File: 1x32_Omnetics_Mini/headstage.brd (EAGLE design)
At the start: 100 x 80 mm, 13 parts, among them U1 RHD2132_QFN

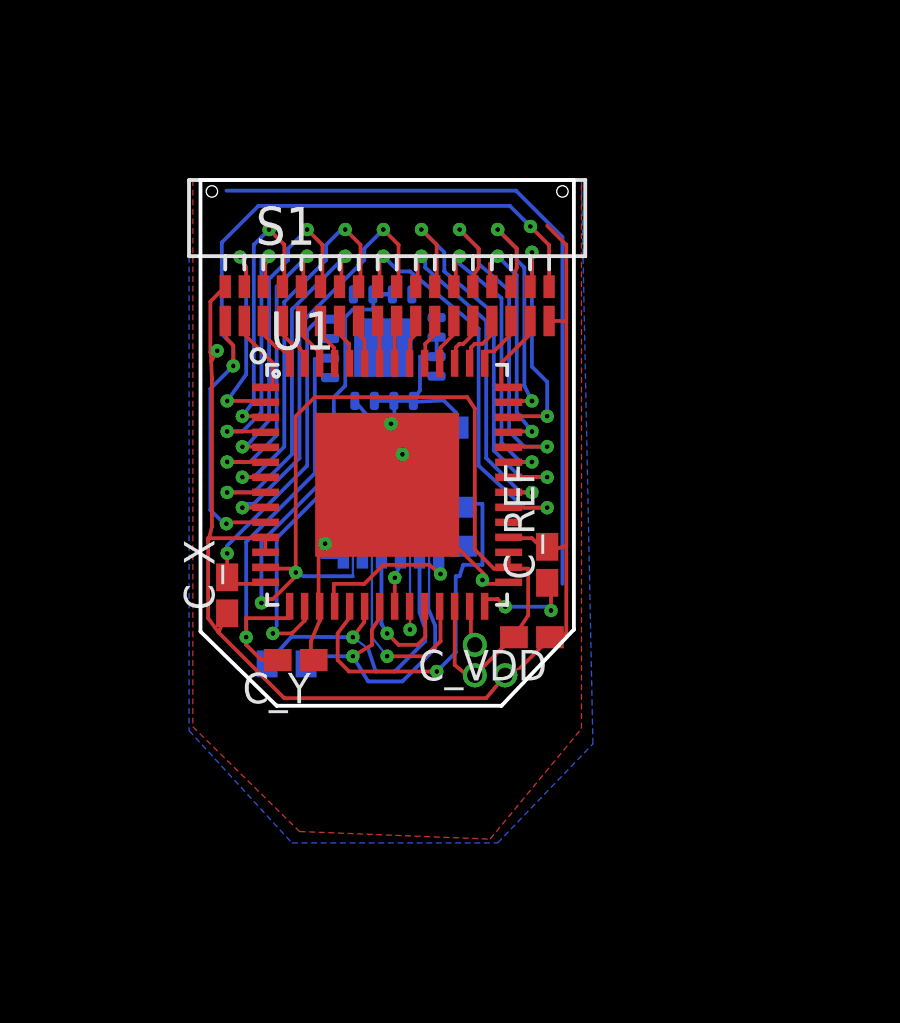
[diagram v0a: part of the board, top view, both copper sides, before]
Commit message: Cleaned up routing
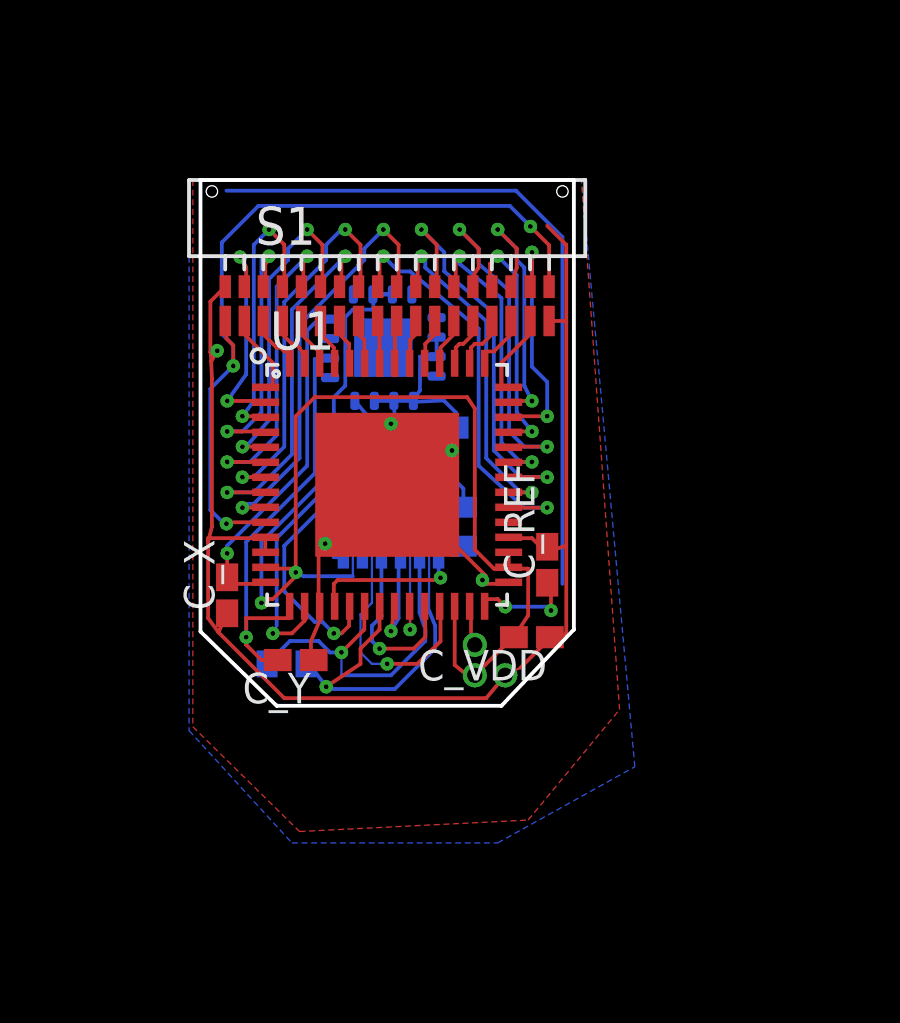
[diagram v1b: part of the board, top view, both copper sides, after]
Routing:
- net MOSI-: track 4.70 -> 6.38 mm
- net SCLK+: track 12.3 -> 13.9 mm
- net MISO1+: track 7.99 -> 8.99 mm
- net CS+: track 13.7 -> 14.6 mm
- net SCLK-: track 10.8 -> 11.7 mm
- net MISO1-: track 5.16 -> 6.00 mm

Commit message: Cosmetic cleanups
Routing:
- net SCLK+: track 13.9 -> 13.3 mm

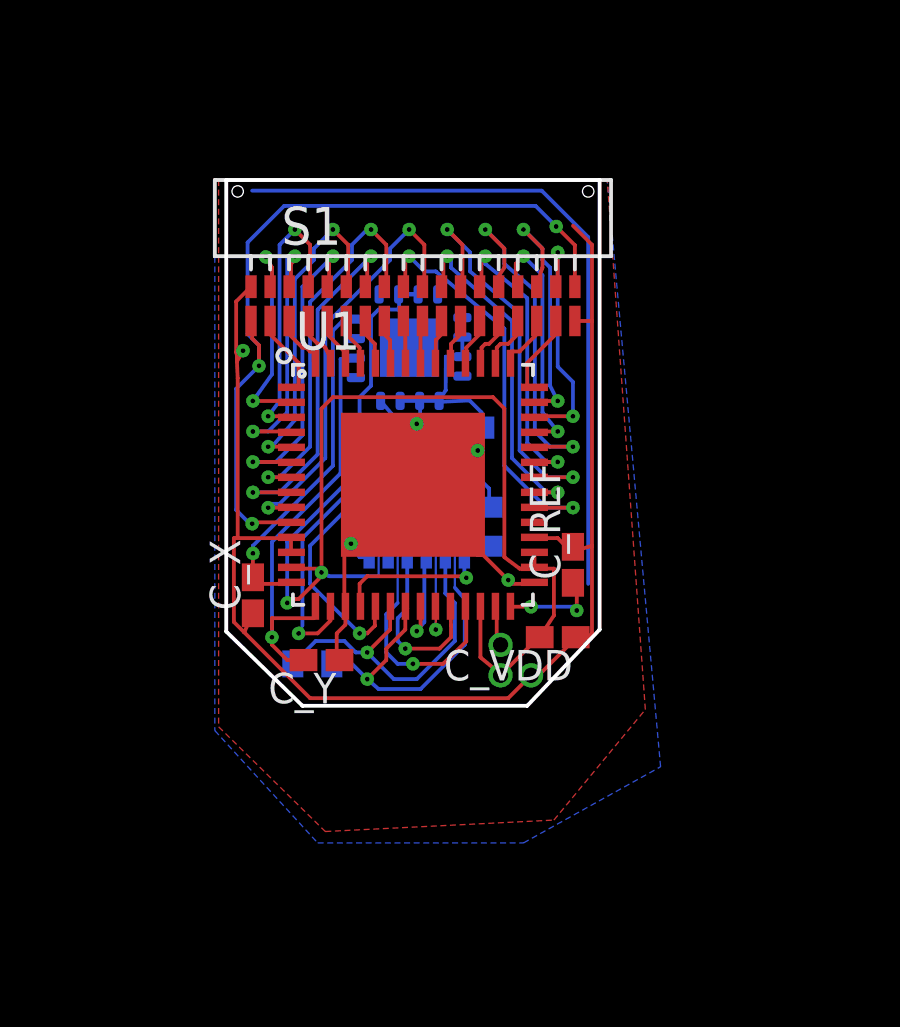
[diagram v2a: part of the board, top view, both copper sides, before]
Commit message: Eliminated one of the non-gnd via under RHD
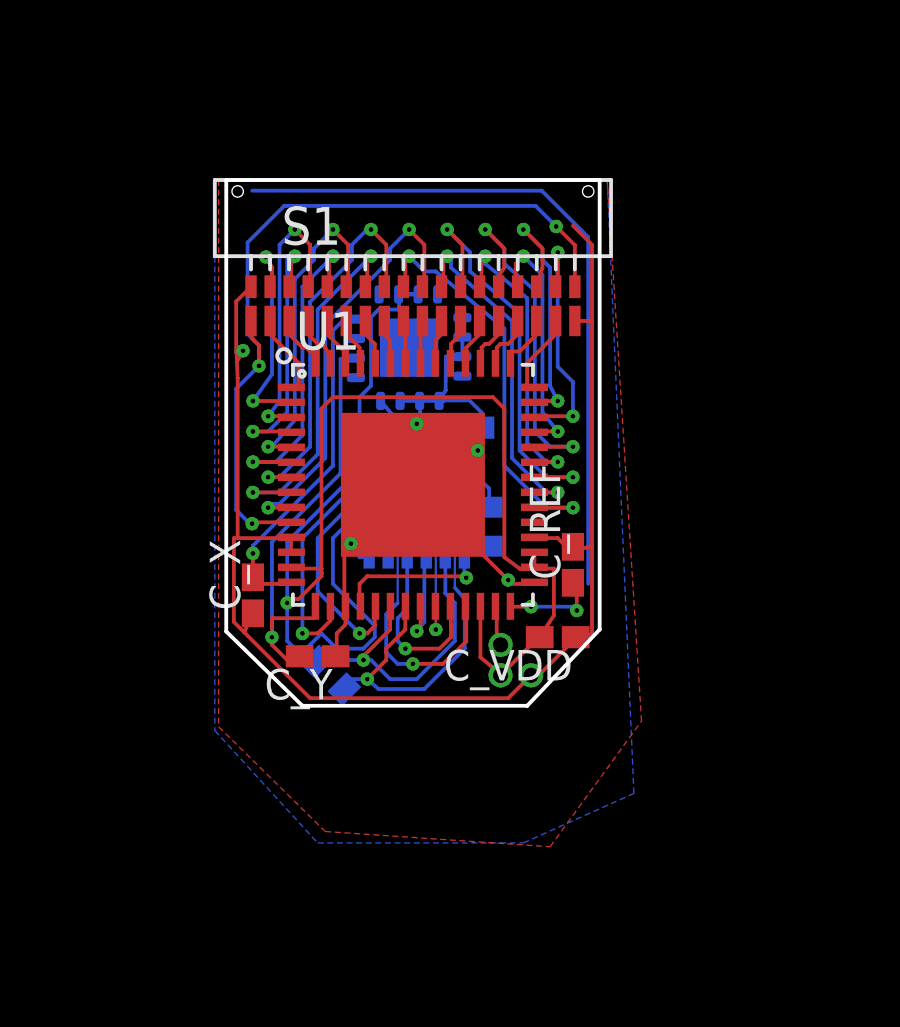
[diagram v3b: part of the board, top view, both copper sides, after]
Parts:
- moved R2 0.72 mm to (15.0, 12.7), turned to 225 degrees
- moved C_Y 0.18 mm to (14.6, 13.3)
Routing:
- net VDD: track 48.0 -> 54.4 mm, vias 3 -> 2
- net SCLK-: track 11.6 -> 10.5 mm
- net SCLK+: track 13.3 -> 12.4 mm

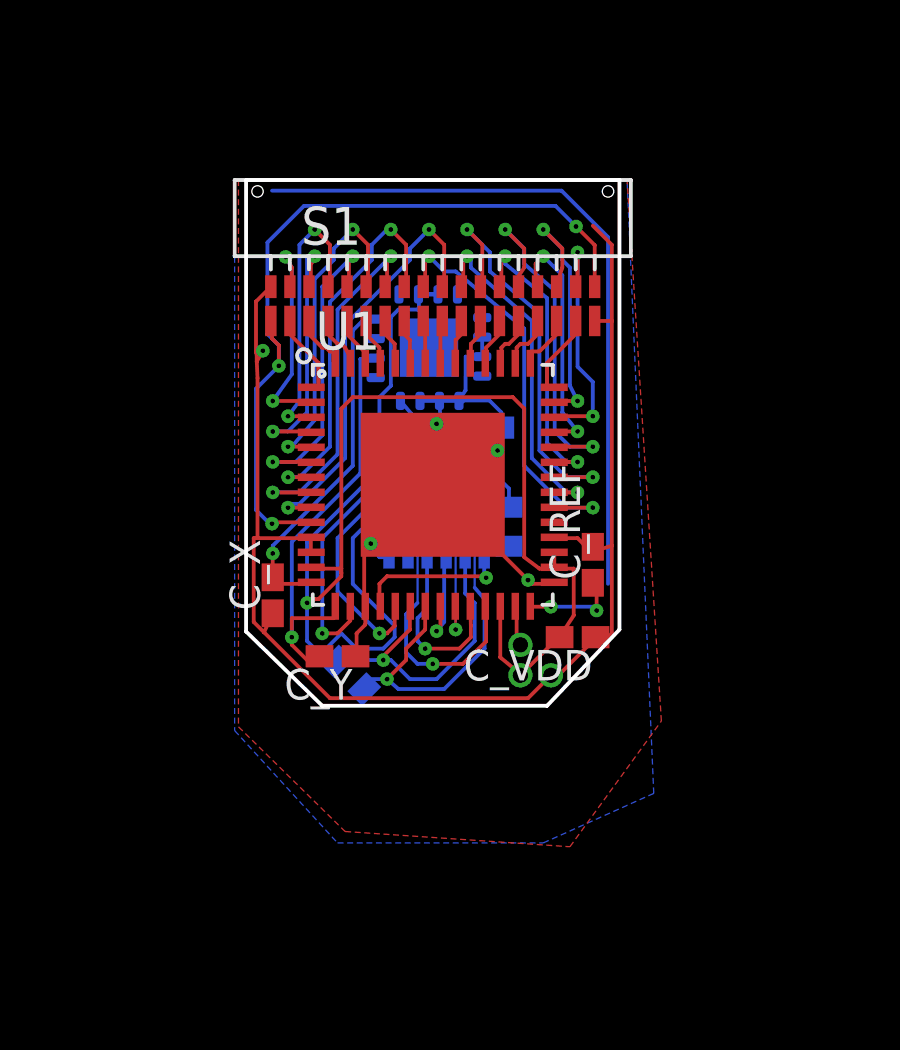
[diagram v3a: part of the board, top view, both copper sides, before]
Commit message: Eliminated 2nd non-gnd via under RHD, all remaining ones are ground and should not cause any issues. There's very likely still a bunch of cleaning to do in order to pass DRCs.
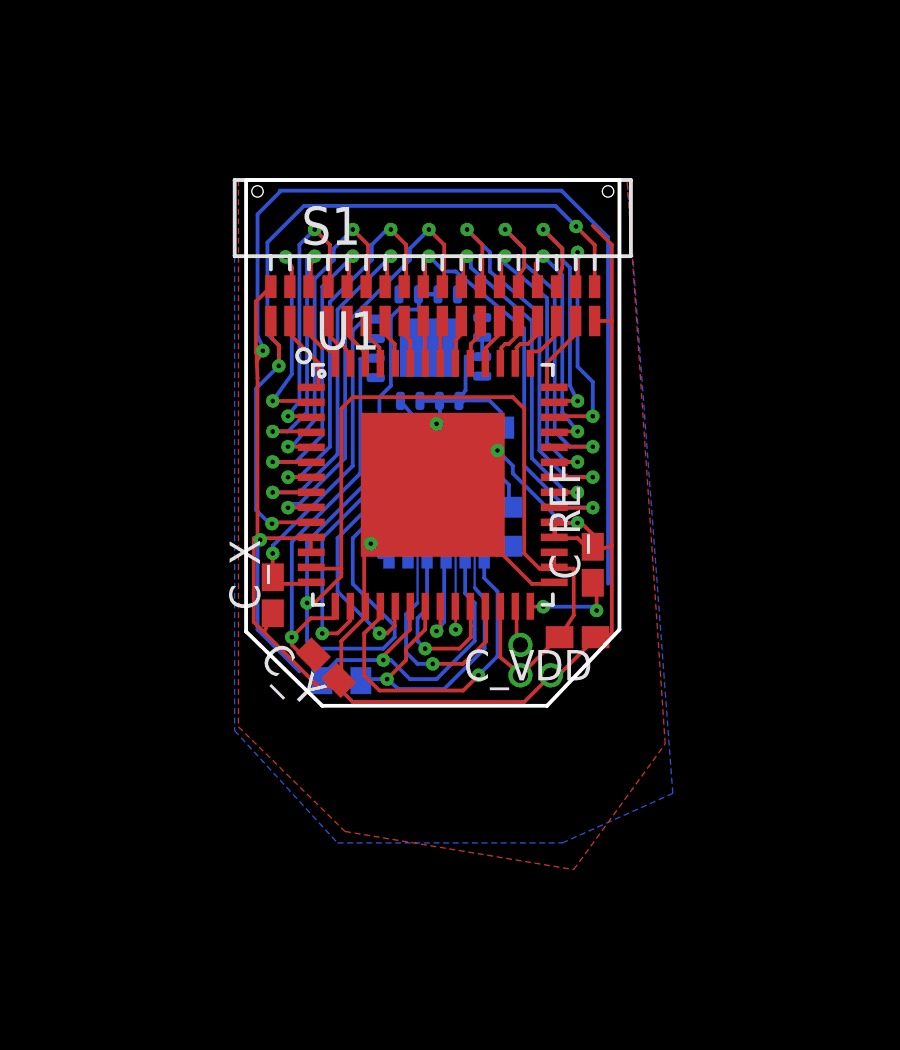
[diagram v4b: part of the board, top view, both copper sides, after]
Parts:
- moved C_Y 0.54 mm to (14.2, 13.0), turned to 135 degrees
- moved R2 0.35 mm to (14.7, 12.5), turned to 180 degrees
- moved R3 0.13 mm to (18.4, 19.2)
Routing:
- net GND: track 93.7 -> 101.6 mm, vias 6 -> 7
- net CS-: track 6.49 -> 12.3 mm
- net N$1: track 0.00 -> 5.71 mm
- net N$2: track 0.00 -> 4.90 mm
- net SCLK-: track 10.5 -> 11.6 mm
